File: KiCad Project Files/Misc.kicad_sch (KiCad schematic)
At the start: 18 parts, among them J2 SWD

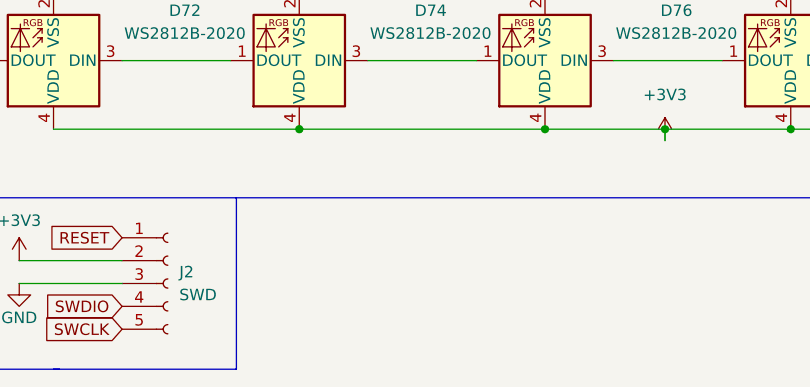
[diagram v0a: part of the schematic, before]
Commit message: QoL Improvements
- Add physical button for Bootloader and Reset.
- Add logic level shifter for the leds according to suggestion by Sleepdealer.
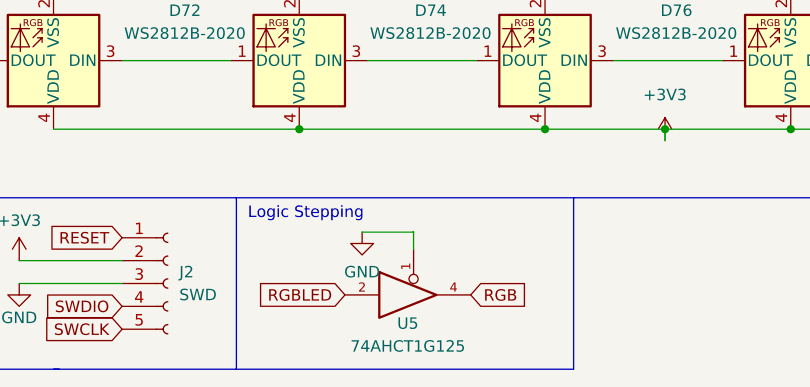
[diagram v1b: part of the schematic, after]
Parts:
- added U5: 74AHCT1G125, Package_TO_SOT_SMD:SOT-23-5, symbol 74xGxx:74AHCT1G125
- D69, D70, D71, D72, D73, D74, D75, D76, D77, D78, D79, D80, D81, D82, D83, D84: footprint LED_SMD:LED_SK6812MINI_PLCC4_3.5x3.5mm_P1.75mm -> acheron_Components:LED_WS2812_2020
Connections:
- net GND: now also U5.1, U5.3 (GND)
- net RGB: now also U5.4
- new net +5V: U5.5 (+5V)
- new net RGBLED: U5.2
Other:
- note added: "Logic Stepping"
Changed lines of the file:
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@@
+    (stroke (width 0) (type default) (color 0 0 0 0))
+  )
+  (polyline (pts (xy 101.6 114.3) (xy 101.6 95.25))
+    (stroke (width 0) (type default) (color 0 0 0 0))
+  )
+  (polyline (pts (xy 64.135 114.3) (xy 101.6 114.3))
+    (stroke (width 0) (type default) (color 0 0 0 0))
+  )
+  (wire (pts (xy 78.105 99.06) (xy 83.82 99.06))
     (stroke (width 0) (type default) (color 0 0 0 0))
   )
@@
     (stroke (width 0) (type default) (color 0 0 0 0))
   )
+  (wire (pts (xy 83.82 99.06) (xy 83.82 100.965))
+    (stroke (width 0) (type default) (color 0 0 0 0))
+  )
   (wire (pts (xy 111.76 87.63) (xy 125.73 87.63))
     (stroke (width 0) (type default) (color 0 0 0 0))
@@
   (polyline (pts (xy 222.25 95.25) (xy 12.7 95.25))
     (stroke (width 0) (type default) (color 0 0 0 0))
+  )
+  (text "Logic Stepping" (at 65.405 97.79 0)
+    (effects (font (size 1.27 1.27)) (justify left bottom))
   )
   (text "Connectors\n" (at 13.335 97.79 0)
@@
   (text "RGB\n" (at 13.335 15.24 0)
     (effects (font (size 1.27 1.27)) (justify left bottom))
+  )
+  (global_label "RGB" (shape input) (at 90.17 106.045 0) (fields_autoplaced)
+    (effects (font (size 1.27 1.27)) (justify left))
+    (property "Intersheet References" "${INTERSHEET_REFS}" (id 0) (at 96.3931 106.1244 0)
+      (effects (font (size 1.27 1.27)) (justify left) hide)
+    )
   )
   (global_label "RGB" (shape input) (at 36.195 29.21 180) (fields_autoplaced)
@@
     )
   )
+  (global_label "RGBLED" (shape input) (at 76.2 106.045 180) (fields_autoplaced)
+    (effects (font (size 1.27 1.27)) (justify right))
+    (property "Intersheet References" "${INTERSHEET_REFS}" (id 0) (at 66.5298 105.9656 0)
+      (effects (font (size 1.27 1.27)) (justify right) hide)
+    )
+  )
   (global_label "RESET" (shape input) (at 51.435 99.695 180) (fields_autoplaced)
     (effects (font (size 1.27 1.27)) (justify right))
@@
     (property "Reference" "D69" (id 0) (at 43.18 40.9448 90))
     (property "Value" "WS2812B-2020" (id 1) (at 43.18 43.4848 90))
-    (property "Footprint" "LED_SMD:LED_SK6812MINI_PLCC4_3.5x3.5mm_P1.75mm" (id 2) (at 36.195 43.815 0)
+    (property "Footprint" "acheron_Components:LED_WS2812_2020" (id 2) (at 36.195 43.815 0)
       (effects (font (size 1.27 1.27)) (justify left top) hide)
     )
@@
     (property "Reference" "D70" (id 0) (at 43.18 58.7248 90))
     (property "Value" "WS2812B-2020" (id 1) (at 43.18 61.2648 90))
-    (property "Footprint" "LED_SMD:LED_SK6812MINI_PLCC4_3.5x3.5mm_P1.75mm" (id 2) (at 36.195 61.595 0)
+    (property "Footprint" "acheron_Components:LED_WS2812_2020" (id 2) (at 36.195 61.595 0)
       (effects (font (size 1.27 1.27)) (justify left top) hide)
     )
@@
     (property "Reference" "D75" (id 0) (at 112.395 24.5999 0))
     (property "Value" "WS2812B-2020" (id 1) (at 112.395 27.1399 0))
-    (property "Footprint" "LED_SMD:LED_SK6812MINI_PLCC4_3.5x3.5mm_P1.75mm" (id 2) (at 99.695 36.83 0)
+    (property "Footprint" "acheron_Components:LED_WS2812_2020" (id 2) (at 99.695 36.83 0)
       (effects (font (size 1.27 1.27)) (justify left top) hide)
     )
@@
     (property "Reference" "D74" (id 0) (at 85.725 74.4599 0))
     (property "Value" "WS2812B-2020" (id 1) (at 85.725 76.9999 0))
-    (property "Footprint" "LED_SMD:LED_SK6812MINI_PLCC4_3.5x3.5mm_P1.75mm" (id 2) (at 69.85 72.39 0)
+    (property "Footprint" "acheron_Components:LED_WS2812_2020" (id 2) (at 69.85 72.39 0)
       (effects (font (size 1.27 1.27)) (justify left top) hide)
     )
@@
     (property "Reference" "D79" (id 0) (at 167.005 24.5999 0))
     (property "Value" "WS2812B-2020" (id 1) (at 167.005 27.1399 0))
-    (property "Footprint" "LED_SMD:LED_SK6812MINI_PLCC4_3.5x3.5mm_P1.75mm" (id 2) (at 154.305 36.83 0)
+    (property "Footprint" "acheron_Components:LED_WS2812_2020" (id 2) (at 154.305 36.83 0)
       (effects (font (size 1.27 1.27)) (justify left top) hide)
     )
@@
     (pin "3")
     (pin "4")
+  )
+  (symbol (lib_id "74xGxx:74AHCT1G125") (at 83.82 106.045 0) (unit 1)
+    (in_bom yes) (on_board yes)
+    (property "Reference" "U5" (id 0) (at 83.185 109.22 0))
+    (property "Value" "74AHCT1G125" (id 1) (at 83.185 111.76 0))
+    (property "Footprint" "Package_TO_SOT_SMD:SOT-23-5" (id 2) (at 83.82 106.045 0)
+      (effects (font (size 1.27 1.27)) hide)
+    )
+    (property "Datasheet" "http://www.ti.com/lit/sg/scyt129e/scyt129e.pdf" (id 3) (at 85.09 117.475 0)
+      (effects (font (size 1.27 1.27)) hide)
+    )
+    (pin "1")
+    (pin "2")
+    (pin "3")
+    (pin "4")
+    (pin "5")
   )
   (symbol (lib_id "power:GND") (at 17.145 107.315 0) (unit 1)
@@
     (property "Reference" "D81" (id 0) (at 194.31 24.5999 0))
     (property "Value" "WS2812B-2020" (id 1) (at 194.31 27.1399 0))
-    (property "Footprint" "LED_SMD:LED_SK6812MINI_PLCC4_3.5x3.5mm_P1.75mm" (id 2) (at 181.61 36.83 0)
+    (property "Footprint" "acheron_Components:LED_WS2812_2020" (id 2) (at 181.61 36.83 0)
       (effects (font (size 1.27 1.27)) (justify left top) hide)
     )
@@
     (property "Reference" "D76" (id 0) (at 113.03 74.4599 0))
     (property "Value" "WS2812B-2020" (id 1) (at 113.03 76.9999 0))
-    (property "Footprint" "LED_SMD:LED_SK6812MINI_PLCC4_3.5x3.5mm_P1.75mm" (id 2) (at 97.155 72.39 0)
+    (property "Footprint" "acheron_Components:LED_WS2812_2020" (id 2) (at 97.155 72.39 0)
       (effects (font (size 1.27 1.27)) (justify left top) hide)
     )
@@
     (property "Reference" "D82" (id 0) (at 194.945 74.4599 0))
     (property "Value" "WS2812B-2020" (id 1) (at 194.945 76.9999 0))
-    (property "Footprint" "LED_SMD:LED_SK6812MINI_PLCC4_3.5x3.5mm_P1.75mm" (id 2) (at 179.07 72.39 0)
+    (property "Footprint" "acheron_Components:LED_WS2812_2020" (id 2) (at 179.07 72.39 0)
       (effects (font (size 1.27 1.27)) (justify left top) hide)
     )
@@
     (property "Reference" "D77" (id 0) (at 139.7 24.5999 0))
     (property "Value" "WS2812B-2020" (id 1) (at 139.7 27.1399 0))
-    (property "Footprint" "LED_SMD:LED_SK6812MINI_PLCC4_3.5x3.5mm_P1.75mm" (id 2) (at 127 36.83 0)
+    (property "Footprint" "acheron_Components:LED_WS2812_2020" (id 2) (at 127 36.83 0)
       (effects (font (size 1.27 1.27)) (justify left top) hide)
     )
@@
     (property "Reference" "D84" (id 0) (at 208.915 56.845 90))
     (property "Value" "WS2812B-2020" (id 1) (at 208.915 59.385 90))
-    (property "Footprint" "LED_SMD:LED_SK6812MINI_PLCC4_3.5x3.5mm_P1.75mm" (id 2) (at 187.325 64.135 0)
+    (property "Footprint" "acheron_Components:LED_WS2812_2020" (id 2) (at 187.325 64.135 0)
       (effects (font (size 1.27 1.27)) (justify left top) hide)
     )
@@
     (pin "1")
   )
+  (symbol (lib_id "power:GND") (at 78.105 99.06 0) (unit 1)
+    (in_bom yes) (on_board yes) (fields_autoplaced)
+    (property "Reference" "#PWR0145" (id 0) (at 78.105 105.41 0)
+      (effects (font (size 1.27 1.27)) hide)
+    )
+    (property "Value" "GND" (id 1) (at 78.105 103.505 0))
+    (property "Footprint" "" (id 2) (at 78.105 99.06 0)
+      (effects (font (size 1.27 1.27)) hide)
+    )
+    (property "Datasheet" "" (id 3) (at 78.105 99.06 0)
+      (effects (font (size 1.27 1.27)) hide)
+    )
+    (pin "1")
+  )
   (symbol (lib_id "cipulot_parts:SK6812MINI") (at 71.12 29.21 0) (unit 1)
     (in_bom yes) (on_board yes) (fields_autoplaced)
     (property "Reference" "D73" (id 0) (at 85.09 24.5999 0))
     (property "Value" "WS2812B-2020" (id 1) (at 85.09 27.1399 0))
-    (property "Footprint" "LED_SMD:LED_SK6812MINI_PLCC4_3.5x3.5mm_P1.75mm" (id 2) (at 72.39 36.83 0)
+    (property "Footprint" "acheron_Components:LED_WS2812_2020" (id 2) (at 72.39 36.83 0)
       (effects (font (size 1.27 1.27)) (justify left top) hide)
     )
@@
     (property "Reference" "D83" (id 0) (at 208.915 39.065 90))
     (property "Value" "WS2812B-2020" (id 1) (at 208.915 41.605 90))
-    (property "Footprint" "LED_SMD:LED_SK6812MINI_PLCC4_3.5x3.5mm_P1.75mm" (id 2) (at 187.325 46.355 0)
+    (property "Footprint" "acheron_Components:LED_WS2812_2020" (id 2) (at 187.325 46.355 0)
       (effects (font (size 1.27 1.27)) (justify left top) hide)
     )
@@
     (property "Reference" "D80" (id 0) (at 167.64 74.4599 0))
     (property "Value" "WS2812B-2020" (id 1) (at 167.64 76.9999 0))
-    (property "Footprint" "LED_SMD:LED_SK6812MINI_PLCC4_3.5x3.5mm_P1.75mm" (id 2) (at 151.765 72.39 0)
+    (property "Footprint" "acheron_Components:LED_WS2812_2020" (id 2) (at 151.765 72.39 0)
       (effects (font (size 1.27 1.27)) (justify left top) hide)
     )
@@
     (property "Reference" "D72" (id 0) (at 58.42 74.4599 0))
     (property "Value" "WS2812B-2020" (id 1) (at 58.42 76.9999 0))
-    (property "Footprint" "LED_SMD:LED_SK6812MINI_PLCC4_3.5x3.5mm_P1.75mm" (id 2) (at 42.545 72.39 0)
+    (property "Footprint" "acheron_Components:LED_WS2812_2020" (id 2) (at 42.545 72.39 0)
       (effects (font (size 1.27 1.27)) (justify left top) hide)
     )
@@
     (property "Reference" "D71" (id 0) (at 57.785 24.5999 0))
     (property "Value" "WS2812B-2020" (id 1) (at 57.785 27.1399 0))
-    (property "Footprint" "LED_SMD:LED_SK6812MINI_PLCC4_3.5x3.5mm_P1.75mm" (id 2) (at 45.085 36.83 0)
+    (property "Footprint" "acheron_Components:LED_WS2812_2020" (id 2) (at 45.085 36.83 0)
       (effects (font (size 1.27 1.27)) (justify left top) hide)
     )
@@
     (property "Reference" "D78" (id 0) (at 140.335 74.4599 0))
     (property "Value" "WS2812B-2020" (id 1) (at 140.335 76.9999 0))
-    (property "Footprint" "LED_SMD:LED_SK6812MINI_PLCC4_3.5x3.5mm_P1.75mm" (id 2) (at 124.46 72.39 0)
-      (effects (font (size 1.27 1.27)) (justify left top) hide)
-    )
+    (property "Footprint" "acheron_Components:LED_WS2812_2020" (id 2) (at 124.46 72.39 0)
+      (effects (font (size 1.27 1.27)) (justify left top) hide)
+    )

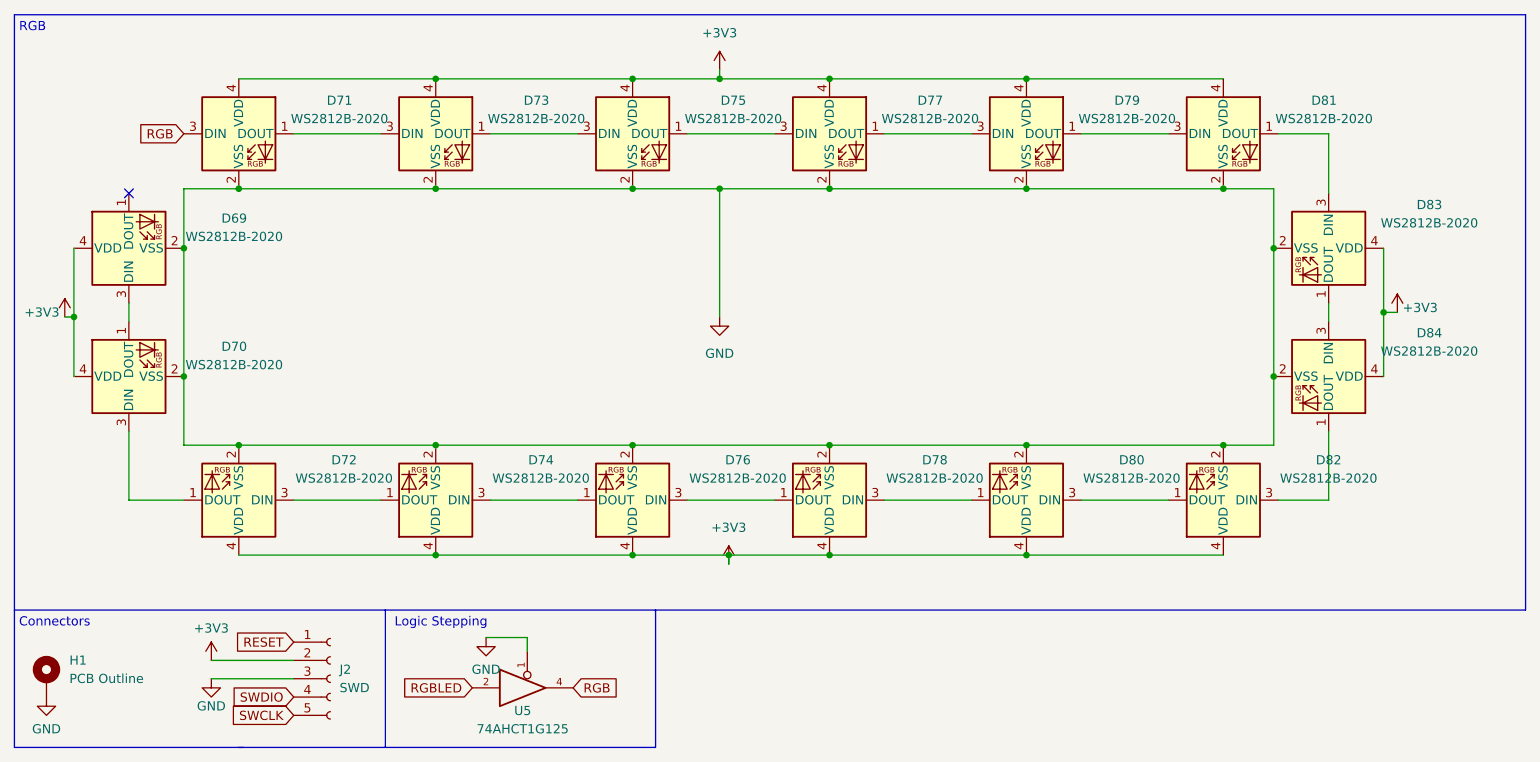
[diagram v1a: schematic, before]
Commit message: Updated LED wiring. Changed production file version scheme.
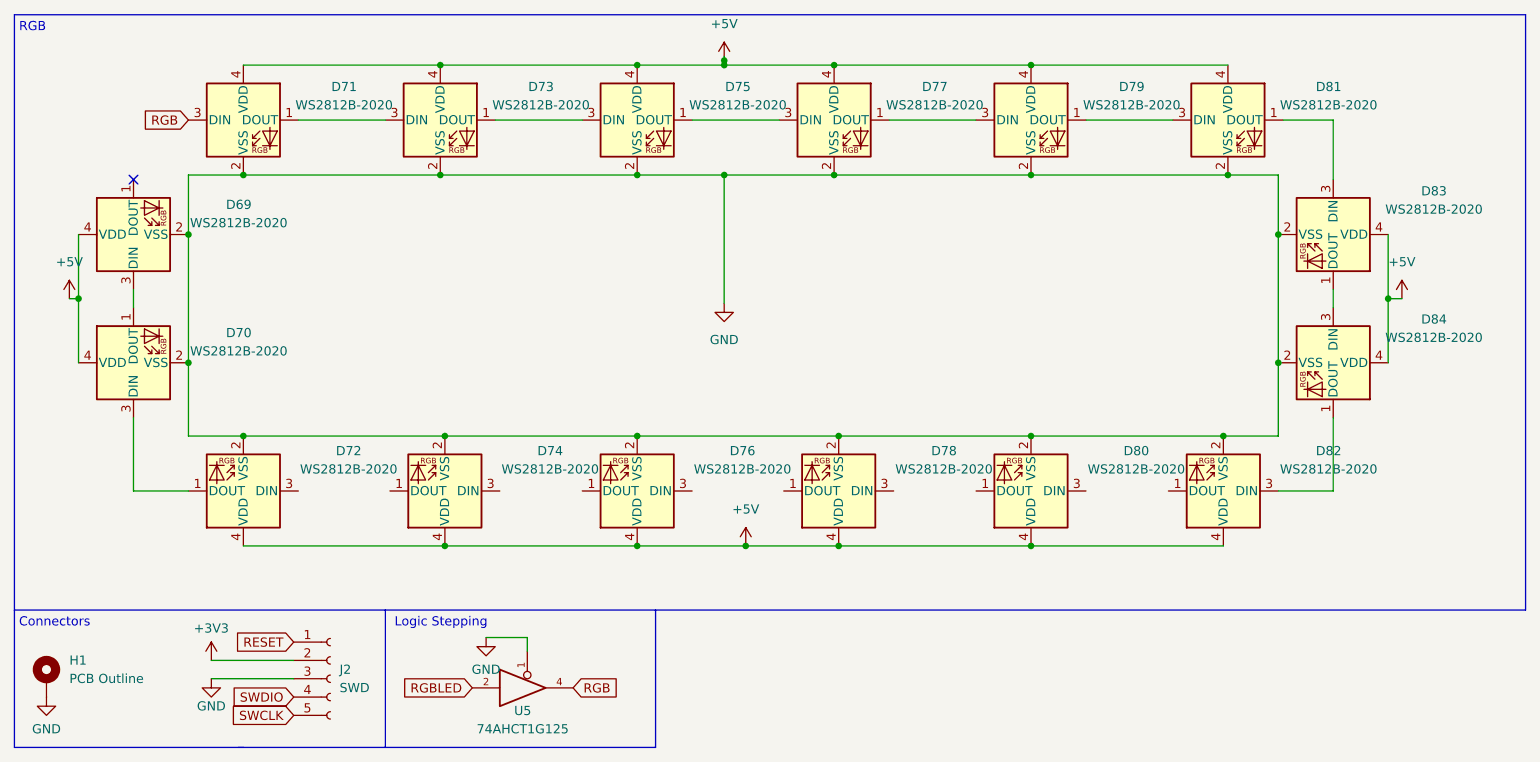
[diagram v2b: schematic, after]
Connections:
- net +3V3: no longer D69.4 (VDD), D70.4 (VDD), D71.4 (VDD), D72.4 (VDD), D73.4 (VDD), D74.4 (VDD), D75.4 (VDD), D76.4 (VDD), D77.4 (VDD), D78.4 (VDD), D79.4 (VDD), D80.4 (VDD), D81.4 (VDD), D82.4 (VDD), D83.4 (VDD), D84.4 (VDD)
- net +5V: now also D69.4 (VDD), D70.4 (VDD), D71.4 (VDD), D72.4 (VDD), D73.4 (VDD), D74.4 (VDD), D75.4 (VDD), D76.4 (VDD), D77.4 (VDD), D78.4 (VDD), D79.4 (VDD), D80.4 (VDD), D81.4 (VDD), D82.4 (VDD), D83.4 (VDD), D84.4 (VDD)
- net at D74.1 (DOUT): no longer D72.3 (DIN)
- net at D74.3 (DIN): no longer D76.1 (DOUT)
- net at D76.3 (DIN): no longer D78.1 (DOUT)
- net at D82.1 (DOUT): no longer D80.3 (DIN)
- net at D80.1 (DOUT): no longer D78.3 (DIN)
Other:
- moved on the sheet: D69, D70, D71, D72, D73, D74, D75, D76, D77, D78, D79, D80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
